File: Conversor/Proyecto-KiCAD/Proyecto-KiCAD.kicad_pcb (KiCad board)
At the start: 2 copper layers, 6 parts, among them Q1 IRFP150, Q2 IRFP150, Q3 IRFP150, Q4 IRFP150, U1 UCC21540, U2 UCC21540

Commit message: Comenzar el layout de componentes de la PCB
- Todos los componentes con footprints asignados (preliminar)
- Organizados los componentes de la placa adaptadora en el esquema del
PCB (usando como guia aproximada la placa adaptadora)
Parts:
- added C1: Csnub1, Capacitor_SMD:C_1206_3216Metric_Pad1.33x1.80mm_HandSolder, F.Cu at (42.6, 256.0)
- added C10: C, Capacitor_SMD:C_1206_3216Metric_Pad1.33x1.80mm_HandSolder, F.Cu at (154.0, 242.6)
- added C11: CDT, Capacitor_SMD:C_1206_3216Metric_Pad1.33x1.80mm_HandSolder, F.Cu at (160.2, 237.2)
- added C12: CDT, Capacitor_SMD:C_1206_3216Metric_Pad1.33x1.80mm_HandSolder, F.Cu at (168.7, 231.0)
- added C13: CVCC, Capacitor_SMD:C_1206_3216Metric_Pad1.33x1.80mm_HandSolder, F.Cu at (148.0, 239.3)
- added C14: CVCC, Capacitor_SMD:C_1206_3216Metric_Pad1.33x1.80mm_HandSolder, F.Cu at (154.0, 239.3)
- added C15: Cboot, Capacitor_SMD:C_1206_3216Metric_Pad1.33x1.80mm_HandSolder, F.Cu at (148.0, 242.6)
- added C16: Cboot, Capacitor_SMD:C_1206_3216Metric_Pad1.33x1.80mm_HandSolder, F.Cu at (180.9, 220.8)
- added C17: CS, Capacitor_SMD:C_1206_3216Metric_Pad1.33x1.80mm_HandSolder, F.Cu at (36.6, 256.0)
- added C18: Cvdd, Capacitor_SMD:C_1206_3216Metric_Pad1.33x1.80mm_HandSolder, F.Cu at (122.1, 261.4)
- added C19: Cvref, Capacitor_SMD:C_1206_3216Metric_Pad1.33x1.80mm_HandSolder, F.Cu at (105.9, 274.8)
- added C2: Csnub2, Capacitor_SMD:C_1206_3216Metric_Pad1.33x1.80mm_HandSolder, F.Cu at (48.6, 256.0)
- added C20: C, Capacitor_SMD:C_1206_3216Metric_Pad1.33x1.80mm_HandSolder, F.Cu at (105.9, 271.4)
- added C21: Cvin, Capacitor_SMD:C_1206_3216Metric_Pad1.33x1.80mm_HandSolder, F.Cu at (110.1, 261.4)
- added C22: C, Capacitor_SMD:C_1206_3216Metric_Pad1.33x1.80mm_HandSolder, F.Cu at (127.0, 254.9)
- added C23: C, Capacitor_SMD:C_1206_3216Metric_Pad1.33x1.80mm_HandSolder, F.Cu at (116.1, 261.4)
- added C24: C4amp, Capacitor_SMD:C_1206_3216Metric_Pad1.33x1.80mm_HandSolder, F.Cu at (111.9, 268.1)
- added C25: C2amp, Capacitor_SMD:C_1206_3216Metric_Pad1.33x1.80mm_HandSolder, F.Cu at (110.1, 264.7)
- added C26: C, Capacitor_SMD:C_1206_3216Metric_Pad1.33x1.80mm_HandSolder, F.Cu at (116.1, 264.7)
- added C27: C, Capacitor_SMD:C_1206_3216Metric_Pad1.33x1.80mm_HandSolder, F.Cu at (105.9, 268.1)
- added C28: CREGIN, Capacitor_SMD:C_1206_3216Metric_Pad1.33x1.80mm_HandSolder, F.Cu at (151.8, 212.6)
- added C29: CREG_IN, Capacitor_SMD:C_1206_3216Metric_Pad1.33x1.80mm_HandSolder, F.Cu at (164.2, 207.0)
- added C3: Csnub3, Capacitor_SMD:C_1206_3216Metric_Pad1.33x1.80mm_HandSolder, F.Cu at (65.4, 245.5)
- added C30: CREG_OUT, Capacitor_SMD:C_1206_3216Metric_Pad1.33x1.80mm_HandSolder, F.Cu at (173.5, 198.3)
- added C31: CFIN, Capacitor_SMD:C_1206_3216Metric_Pad1.33x1.80mm_HandSolder, F.Cu at (181.2, 188.6)
- added C32: CBYPASS, Capacitor_SMD:C_1206_3216Metric_Pad1.33x1.80mm_HandSolder, F.Cu at (145.8, 212.6)
- added C33: CREGOUT, Capacitor_SMD:C_1206_3216Metric_Pad1.33x1.80mm_HandSolder, F.Cu at (157.9, 212.6)
- added C34: 0.1uF, Capacitor_SMD:C_1206_3216Metric_Pad1.33x1.80mm_HandSolder, F.Cu at (368.6, 181.6)
- added C35: 0.1uF, Capacitor_SMD:C_1206_3216Metric_Pad1.33x1.80mm_HandSolder, F.Cu at (373.7, 175.3)
- added C36: 0.1uF, Capacitor_SMD:C_1206_3216Metric_Pad1.33x1.80mm_HandSolder, F.Cu at (358.1, 153.7)
- added C37: 27pF, Capacitor_SMD:C_1206_3216Metric_Pad1.33x1.80mm_HandSolder, F.Cu at (378.5, 167.6)
- added C38: 27pF, Capacitor_SMD:C_1206_3216Metric_Pad1.33x1.80mm_HandSolder, F.Cu at (378.5, 162.6)
- added C39: 1uF, Capacitor_SMD:C_1206_3216Metric_Pad1.33x1.80mm_HandSolder, F.Cu at (337.8, 160.0)
- added C4: Csnub4, Capacitor_SMD:C_1206_3216Metric_Pad1.33x1.80mm_HandSolder, F.Cu at (71.3, 236.1)
- added C40: 10nF, Capacitor_SMD:C_1206_3216Metric_Pad1.33x1.80mm_HandSolder, F.Cu at (364.5, 186.7)
- added C41: 0.1uF, Capacitor_SMD:C_1206_3216Metric_Pad1.33x1.80mm_HandSolder, F.Cu at (342.9, 152.4)
- added C42: 0.1uF, Capacitor_SMD:C_1206_3216Metric_Pad1.33x1.80mm_HandSolder, F.Cu at (339.1, 152.4)
- added C43: 10uF, Capacitor_THT:CP_Radial_D6.3mm_P2.50mm, F.Cu at (331.5, 153.7)
- added C44: 10nF, Capacitor_SMD:C_1206_3216Metric_Pad1.33x1.80mm_HandSolder, F.Cu at (330.2, 163.8)
- added C45: 0.1uF, Capacitor_SMD:C_1206_3216Metric_Pad1.33x1.80mm_HandSolder, F.Cu at (365.8, 161.3)
- added C46: 2.2uF, Capacitor_THT:CP_Radial_D6.3mm_P2.50mm, F.Cu at (341.6, 165.1)
- added C47: 33nF, Capacitor_SMD:C_1206_3216Metric_Pad1.33x1.80mm_HandSolder, F.Cu at (349.2, 162.6)
- added C5: Cin, Capacitor_THT:CP_Radial_D6.3mm_P2.50mm, F.Cu at (83.0, 223.1)
- added C6: Cf, Capacitor_THT:CP_Radial_D18.0mm_P7.50mm, F.Cu at (28.4, 228.9)
- added C7: C, Capacitor_SMD:C_1206_3216Metric_Pad1.33x1.80mm_HandSolder, F.Cu at (160.0, 240.5)
- added C8: C, Capacitor_SMD:C_1206_3216Metric_Pad1.33x1.80mm_HandSolder, F.Cu at (166.2, 237.2)
- added C9: C, Capacitor_SMD:C_1206_3216Metric_Pad1.33x1.80mm_HandSolder, F.Cu at (174.7, 231.0)
- added D1: MUR860, Package_TO_SOT_THT:TO-220F-2_Vertical, F.Cu at (45.3, 229.6)
- added D2: MUR860, Package_TO_SOT_THT:TO-220F-2_Vertical, F.Cu at (45.3, 235.8)
- added D3: MUR860, Package_TO_SOT_THT:TO-220F-2_Vertical, F.Cu at (25.2, 255.7)
- added D4: MUR860, Package_TO_SOT_THT:TO-220F-2_Vertical, F.Cu at (62.7, 223.0)
- added D5: MBR0520, Diode_SMD:D_SOD-123, F.Cu at (123.8, 268.1)
- added J1: ConnPila, TerminalBlock:TerminalBlock_bornier-2_P5.08mm, F.Cu at (42.5, 249.8)
- added J2: ConnTrafoP, TerminalBlock:TerminalBlock_bornier-2_P5.08mm, F.Cu at (68.5, 229.9)
- added J3: ConnTrafoS, TerminalBlock:TerminalBlock_bornier-2_P5.08mm, F.Cu at (54.0, 249.8)
- added J4: ConnLf, TerminalBlock:TerminalBlock_bornier-2_P5.08mm, F.Cu at (60.0, 239.3)
- added J5: ConnCarga, TerminalBlock:TerminalBlock_bornier-2_P5.08mm, F.Cu at (57.0, 230.3)
- added J6: Barrel_Jack_Switch, Connector_BarrelJack:BarrelJack_GCT_DCJ200-10-A_Horizontal, F.Cu at (297.8, 39.3)
- added J7: DIMM100, 5390213-1:TE_5390213-1, F.Cu at (320.0, 119.4)
- added LED1: Led smd, Diode_SMD:D_1206_3216Metric_Pad1.42x1.75mm_HandSolder, F.Cu at (307.3, 106.7)
- added LED2: Led smd, Diode_SMD:D_1206_3216Metric_Pad1.42x1.75mm_HandSolder, F.Cu at (307.3, 111.8)
- added LED3: Led smd, Diode_SMD:D_1206_3216Metric_Pad1.42x1.75mm_HandSolder, F.Cu at (307.3, 116.8)
- added LED4: Led smd, Diode_SMD:D_1206_3216Metric_Pad1.42x1.75mm_HandSolder, F.Cu at (307.3, 121.9)
- added LED5: Led smd, Diode_SMD:D_1206_3216Metric_Pad1.42x1.75mm_HandSolder, F.Cu at (344.2, 179.1)
- added LED6: Led smd, Diode_SMD:D_1206_3216Metric_Pad1.42x1.75mm_HandSolder, F.Cu at (344.2, 175.3)
- added P1: SW_SPDT, Connector_PinHeader_2.54mm:PinHeader_1x03_P2.54mm_Vertical, F.Cu at (175.9, 189.2)
- added P10: Header GPIO, Connector_PinHeader_2.54mm:PinHeader_1x08_P2.54mm_Vertical, F.Cu at (348.6, 106.7)
- added P11: Header SD, Connector_PinSocket_2.54mm:PinSocket_1x06_P2.54mm_Horizontal, F.Cu at (356.9, 121.9)
- added P12: USB-B, Connector_USB:USB_B_Lumberg_2411_02_Horizontal, F.Cu at (359.4, 190.1)
- added P2: 5V Header, Connector_PinHeader_2.54mm:PinHeader_1x02_P2.54mm_Vertical, F.Cu at (188.1, 181.2)
- added P3: 5V Header, Connector_PinHeader_2.54mm:PinHeader_1x02_P2.54mm_Vertical, F.Cu at (168.2, 197.9)
- added P4: Jumper 2, Connector_PinHeader_2.54mm:PinHeader_1x03_P2.54mm_Vertical, F.Cu at (163.6, 197.9)
- added P5: Header 7X2, Connector_PinSocket_2.54mm:PinSocket_2x07_P2.54mm_Vertical, F.Cu at (287.0, 101.6)
- added P6: Header UART, Connector_PinHeader_2.54mm:PinHeader_1x04_P2.54mm_Vertical, F.Cu at (348.0, 133.4)
- added P7: Header I2C, Connector_PinHeader_2.54mm:PinHeader_1x04_P2.54mm_Vertical, F.Cu at (363.2, 133.4)
- added P8: Header PWM, Connector_PinHeader_2.54mm:PinHeader_1x08_P2.54mm_Vertical, F.Cu at (363.2, 78.8)
- added P9: Header ADC, Connector_PinHeader_2.54mm:PinHeader_1x05_P2.54mm_Vertical, F.Cu at (348.0, 82.5)
- added Q5: IRF7425, Package_SO:SOIC-8_3.9x4.9mm_P1.27mm, F.Cu at (364.8, 175.3)
- added R1: RonH, Resistor_SMD:R_1206_3216Metric_Pad1.30x1.75mm_HandSolder, F.Cu at (166.0, 240.5)
- added R10: 0, Resistor_SMD:R_1206_3216Metric_Pad1.30x1.75mm_HandSolder, F.Cu at (164.2, 210.3)
- added R11: Rpu, Resistor_SMD:R_1206_3216Metric_Pad1.30x1.75mm_HandSolder, F.Cu at (117.8, 274.6)
- added R12: R1amp, Resistor_SMD:R_1206_3216Metric_Pad1.30x1.75mm_HandSolder, F.Cu at (117.9, 268.1)
- added R13: R3amp, Resistor_SMD:R_1206_3216Metric_Pad1.30x1.75mm_HandSolder, F.Cu at (128.0, 264.8)
- added R14: R4amp, Resistor_SMD:R_1206_3216Metric_Pad1.30x1.75mm_HandSolder, F.Cu at (117.9, 271.3)
- added R15: 0, Resistor_SMD:R_1206_3216Metric_Pad1.30x1.75mm_HandSolder, F.Cu at (188.7, 187.7)
- added R16: R2amp, Resistor_SMD:R_1206_3216Metric_Pad1.30x1.75mm_HandSolder, F.Cu at (132.9, 254.9)
- added R17: 0, Resistor_SMD:R_1206_3216Metric_Pad1.30x1.75mm_HandSolder, F.Cu at (193.4, 180.5)
- added R18: Rpu, Resistor_SMD:R_1206_3216Metric_Pad1.30x1.75mm_HandSolder, F.Cu at (128.1, 261.5)
- added R19: Rpu, Resistor_SMD:R_1206_3216Metric_Pad1.30x1.75mm_HandSolder, F.Cu at (122.1, 264.7)
- added R2: RonL, Resistor_SMD:R_1206_3216Metric_Pad1.30x1.75mm_HandSolder, F.Cu at (180.9, 224.2)
- added R20: R, Resistor_SMD:R_1206_3216Metric_Pad1.30x1.75mm_HandSolder, F.Cu at (128.1, 258.2)
- added R21: 220, Resistor_SMD:R_1206_3216Metric_Pad1.30x1.75mm_HandSolder, F.Cu at (301.2, 106.7)
- added R22: 1k, Resistor_SMD:R_1206_3216Metric_Pad1.30x1.75mm_HandSolder, F.Cu at (281.8, 129.8)
- added R23: 220, Resistor_SMD:R_1206_3216Metric_Pad1.30x1.75mm_HandSolder, F.Cu at (301.2, 111.8)
- added R24: 1k, Resistor_SMD:R_1206_3216Metric_Pad1.30x1.75mm_HandSolder, F.Cu at (281.8, 140.2)
- added R25: 220, Resistor_SMD:R_1206_3216Metric_Pad1.30x1.75mm_HandSolder, F.Cu at (301.2, 116.8)
- added R26: 1k, Resistor_SMD:R_1206_3216Metric_Pad1.30x1.75mm_HandSolder, F.Cu at (281.8, 150.4)
- added R27: 220, Resistor_SMD:R_1206_3216Metric_Pad1.30x1.75mm_HandSolder, F.Cu at (301.2, 121.9)
- added R28: 1k, Resistor_SMD:R_1206_3216Metric_Pad1.30x1.75mm_HandSolder, F.Cu at (281.8, 160.6)
- added R29: 1k, Resistor_SMD:R_1206_3216Metric_Pad1.30x1.75mm_HandSolder, F.Cu at (362.2, 181.6)
- added R3: RonH, Resistor_SMD:R_1206_3216Metric_Pad1.30x1.75mm_HandSolder, F.Cu at (180.9, 227.4)
- added R30: 470, Resistor_SMD:R_1206_3216Metric_Pad1.30x1.75mm_HandSolder, F.Cu at (132.6, 241.8)
- added R31: 1k, Resistor_SMD:R_1206_3216Metric_Pad1.30x1.75mm_HandSolder, F.Cu at (349.2, 156.2)
- added R32: 27, Resistor_SMD:R_1206_3216Metric_Pad1.30x1.75mm_HandSolder, F.Cu at (356.2, 184.4)
- added R33: 27, Resistor_SMD:R_1206_3216Metric_Pad1.30x1.75mm_HandSolder, F.Cu at (353.1, 184.4)
- added R34: 1k5, Resistor_SMD:R_1206_3216Metric_Pad1.30x1.75mm_HandSolder, F.Cu at (351.5, 179.5)
- added R35: 220, Resistor_SMD:R_1206_3216Metric_Pad1.30x1.75mm_HandSolder, F.Cu at (337.8, 179.1)
- added R36: 220, Resistor_SMD:R_1206_3216Metric_Pad1.30x1.75mm_HandSolder, F.Cu at (337.8, 175.3)
- added R37: Rfix, Resistor_SMD:R_1206_3216Metric_Pad1.30x1.75mm_HandSolder, F.Cu at (181.2, 191.9)
- added R38: Rfix, Resistor_SMD:R_1206_3216Metric_Pad1.30x1.75mm_HandSolder, F.Cu at (111.9, 271.4)
- added R4: RonL, Resistor_SMD:R_1206_3216Metric_Pad1.30x1.75mm_HandSolder, F.Cu at (180.7, 231.0)
- added R5: RS, Resistor_SMD:R_1206_3216Metric_Pad1.30x1.75mm_HandSolder, F.Cu at (172.2, 234.4)
- added R6: RS, Resistor_SMD:R_1206_3216Metric_Pad1.30x1.75mm_HandSolder, F.Cu at (186.9, 220.8)
- added R7: RS, Resistor_SMD:R_2512_6332Metric_Pad1.40x3.35mm_HandSolder, F.Cu at (75.7, 221.6)
- added R8: Rpu, Resistor_SMD:R_1206_3216Metric_Pad1.30x1.75mm_HandSolder, F.Cu at (111.9, 274.7)
- added R9: Rpu, Resistor_SMD:R_1206_3216Metric_Pad1.30x1.75mm_HandSolder, F.Cu at (134.0, 258.2)
- added SW1: Switch, Button_Switch_THT:SW_PUSH_6mm, F.Cu at (294.6, 134.3)
- added SW2: Switch, Button_Switch_THT:SW_PUSH_6mm, F.Cu at (294.6, 144.8)
- added SW3: Switch, Button_Switch_THT:SW_PUSH_6mm, F.Cu at (294.6, 154.9)
- added SW4: Switch, Button_Switch_THT:SW_PUSH_6mm, F.Cu at (294.6, 165.1)
- added SW5: Switch, Button_Switch_THT:SW_PUSH_6mm, F.Cu at (362.5, 151.4)
- added U10: OPA365xxD, Package_SO:SOIC-8_3.9x4.9mm_P1.27mm, F.Cu at (111.3, 256.5)
- added U11: LM7805_TO252, Package_TO_SOT_SMD:TO-252-2, F.Cu at (179.7, 182.9)
- added U12: ACPL-P480, Package_SO:SSO-6_6.8x4.6mm_P1.27mm_Clearance7mm, F.Cu at (163.3, 222.2)
- added U13: THB3-1211, Package_DIP:DIP-24_W15.24mm, F.Cu at (289.6, 49.5)
- added U14: FT232BL, Package_QFP:LQFP-48_7x7mm_P0.5mm, F.Cu at (358.1, 165.1)
- added U15: LP2985-3.3, Package_TO_SOT_SMD:SOT-23-5, F.Cu at (335.4, 164.5)
- added U3: ACPL-P480, Package_SO:SSO-6_6.8x4.6mm_P1.27mm_Clearance7mm, F.Cu at (151.1, 234.5)
- added U4: ACPL-P480, Package_SO:SSO-6_6.8x4.6mm_P1.27mm_Clearance7mm, F.Cu at (151.1, 222.2)
- added U5: 2ED21834-S06J, Package_SO:SO-14_3.9x8.65mm_P1.27mm, F.Cu at (161.4, 230.4)
- added U6: 2ED21834-S06J, Package_SO:SO-14_3.9x8.65mm_P1.27mm, F.Cu at (173.7, 224.3)
- added U7: TMCS1100A4, Package_SO:SOIC-8_3.9x4.9mm_P1.27mm, F.Cu at (119.7, 256.5)
- added U8: LM5056APMH/NOPB, Package_SO:HTSSOP-28-1EP_4.4x9.7mm_P0.65mm_EP2.85x5.4mm, F.Cu at (98.5, 270.7)
- added U9: ISO7242C, Package_SO:SOIC-16W_7.5x10.3mm_P1.27mm, F.Cu at (100.6, 259.2)
- added Y1: 6 MHz, Crystal:Crystal_HC18-U_Vertical, F.Cu at (370.8, 167.6)
- Q1, Q2, Q3, Q4: footprint Package_TO_SOT_THT:TO-247-3_Horizontal_TabDown -> Package_TO_SOT_THT:TO-247-3_Vertical
- U1: value UCC21540 -> LP2985-3.3; footprint Package_SO:SOIC-16W_7.5x10.3mm_P1.27mm -> Package_TO_SOT_SMD:SOT-23-5
- U2: value UCC21540 -> ACPL-P480; footprint Package_SO:SOIC-16W_7.5x10.3mm_P1.27mm -> Package_SO:SSO-6_6.8x4.6mm_P1.27mm_Clearance7mm
- moved Q1 180.8 mm to (25.1, 241.8)
- moved Q4 180.8 mm to (42.5, 241.8)
- moved Q2 164.7 mm to (25.1, 248.4)
- moved Q3 141.7 mm to (45.2, 222.3)
- moved U2 112.4 mm to (151.1, 228.4)
- moved U1 101.0 mm to (180.8, 195.8)
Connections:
- Q1 pad 1: Net-(Q1-Pad1) -> Net-(C1-Pad1)
- Q1 pad 2: Net-(Q1-Pad2) -> /Conversor/GATE1
- Q1 pad 3: Net-(Q1-Pad3) -> /Conversor/S1D3
- Q2 pad 1: Net-(Q1-Pad3) -> Net-(C1-Pad1)
- Q2 pad 2: Net-(Q2-Pad2) -> /Conversor/GATE2
- Q2 pad 3: Net-(Q2-Pad3) -> /Conversor/S2D4
- Q3 pad 1: Net-(Q1-Pad1) -> /Conversor/S1D3
- Q3 pad 2: Net-(Q3-Pad2) -> /Conversor/GATE3
- Q3 pad 3: Net-(Q3-Pad3) -> GND1
- Q4 pad 1: Net-(Q3-Pad3) -> /Conversor/S2D4
- Q4 pad 2: Net-(Q4-Pad2) -> /Conversor/GATE4
- Q4 pad 3: Net-(Q2-Pad3) -> GND1
- U1 pad 1: unconnected-(U1-Pad1) -> +5VD
- U1 pad 2: unconnected-(U1-Pad2) -> GNDD
- U1 pad 3: unconnected-(U1-Pad3) -> +5VD
- U1 pad 4: unconnected-(U1-Pad4) -> Net-(C32-Pad1)
- U1 pad 5: unconnected-(U1-Pad5) -> +3.3V
- U2 pad 1: unconnected-(U2-Pad1) -> /Drivers y Optos/PWM1
- U2 pad 3: unconnected-(U2-Pad3) -> GNDD
- U2 pad 4: unconnected-(U2-Pad4) -> GND1
- U2 pad 5: unconnected-(U2-Pad5) -> (no net)
- U2 pad 6: unconnected-(U2-Pad6) -> +5VP

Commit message: Reempezar el ordenado de componentes del PCB
- Intentar copiar mas a la placa adaptadora en la parte del DSP (digital)
  - Algunas cosas (como los headers y la parte de USB) se movieron para hacer entrar mejor las cosas
- Layout bastante completo
- Agregados algunos modelos 3D faltantes
Por hacer:
  - Mover y reorganizar la parte del LM5056, porque tiene una pata que va al secundario, y ahora esta muy lejos del area de GND2
  - Ver como reorganizar un poco para que no queden esquinas vacias
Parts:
- added R39: Rfix, Resistor_SMD:R_1206_3216Metric_Pad1.30x1.75mm_HandSolder, F.Cu at (104.1, 216.5)
- added R7: RS, Resistor_SMD:R_2512_6332Metric_Pad1.40x3.35mm_HandSolder, F.Cu at (67.9, 203.2)
- C10, C17, C18, C19, C34, C36, C37, C38, C40, C45, C47, C7, C8, C9, R1, R10, R15, R17, R19, R2, R29, R3, R31, R4, R9: moved to B.Cu
- C43: footprint Capacitor_THT:CP_Radial_D6.3mm_P2.50mm -> Capacitor_THT:CP_Radial_D4.0mm_P1.50mm
- C46: footprint Capacitor_THT:CP_Radial_D6.3mm_P2.50mm -> Capacitor_THT:CP_Radial_D4.0mm_P2.00mm
- U14: footprint Package_QFP:LQFP-48_7x7mm_P0.5mm -> Package_DFN_QFN:QFN-32-1EP_7x7mm_P0.65mm_EP5.4x5.4mm
- moved C38 262.0 mm to (116.8, 176.5), turned to 90 degrees
- moved C37 256.7 mm to (121.9, 176.5), turned to 90 degrees
- moved Y1 251.9 mm to (119.4, 183.0), turned to -90 degrees
- moved C45 238.5 mm to (129.0, 190.0), turned to 180 degrees
- moved SW5 235.9 mm to (127.6, 173.0)
- moved D3 231.6 mm to (150.6, 61.0), turned to 90 degrees
- moved P8 231.4 mm to (140.3, 141.0)
- moved C40 230.5 mm to (134.6, 203.2)
- moved LED6 227.3 mm to (118.1, 198.8), turned to -90 degrees
- moved U14 226.7 mm to (132.7, 188.5), turned to 90 degrees
- moved P12 226.7 mm to (133.3, 206.6)
- moved LED5 224.4 mm to (120.7, 198.8), turned to -90 degrees
- moved R36 221.7 mm to (118.1, 205.1), turned to 90 degrees
- moved R34 221.4 mm to (130.8, 196.8), turned to 90 degrees
- moved J3 221.0 mm to (160.0, 55.9)
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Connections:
- C1 pad 1: Net-(C1-Pad1) -> /Conversor/IFC-
- C17 pad 1: /Conversor/IFC+ -> /Conversor/VFC
- C2 pad 1: Net-(C1-Pad1) -> /Conversor/IFC-
- C33 pad 1: +3.3V -> +3V3
- C5 pad 1: Net-(C1-Pad1) -> /Conversor/IFC-
- D1 pad 1: (no net) -> Net-(D1-Pad1)
- D1 pad 2: (no net) -> Net-(D1-Pad2)
- D2 pad 1: (no net) -> Net-(D2-Pad1)
- D2 pad 2: (no net) -> Net-(D1-Pad2)
- D3 pad 1: (no net) -> GND2
- D3 pad 2: (no net) -> Net-(D1-Pad1)
- D4 pad 1: (no net) -> GND2
- D4 pad 2: (no net) -> Net-(D2-Pad1)
- J3 pad 1: Net-(D1-Pad3) -> Net-(D1-Pad1)
- J3 pad 2: Net-(D2-Pad3) -> Net-(D2-Pad1)
- J4 pad 1: Net-(D1-Pad4) -> Net-(D1-Pad2)
- Q1 pad 1: Net-(C1-Pad1) -> /Conversor/IFC-
- Q2 pad 1: Net-(C1-Pad1) -> /Conversor/IFC-
- U1 pad 5: +3.3V -> +3V3
- U12 pad 5: (no net) -> Net-(U12-Pad5)
- U2 pad 5: (no net) -> Net-(U2-Pad5)
- U3 pad 5: (no net) -> Net-(U3-Pad5)
- U4 pad 5: (no net) -> Net-(U4-Pad5)
- U5 pad 1: Net-(U2-Pad4) -> Net-(U2-Pad5)
- U5 pad 2: Net-(U3-Pad4) -> Net-(U3-Pad5)
- U6 pad 1: Net-(U4-Pad4) -> Net-(U4-Pad5)
- U6 pad 2: Net-(U12-Pad4) -> Net-(U12-Pad5)
- U8 pad 16: (no net) -> Net-(R38-Pad1)
- U8 pad 22: (no net) -> Net-(U8-Pad22)
- U8 pad 4: /Conversor/IFC+ -> /Conversor/VFC

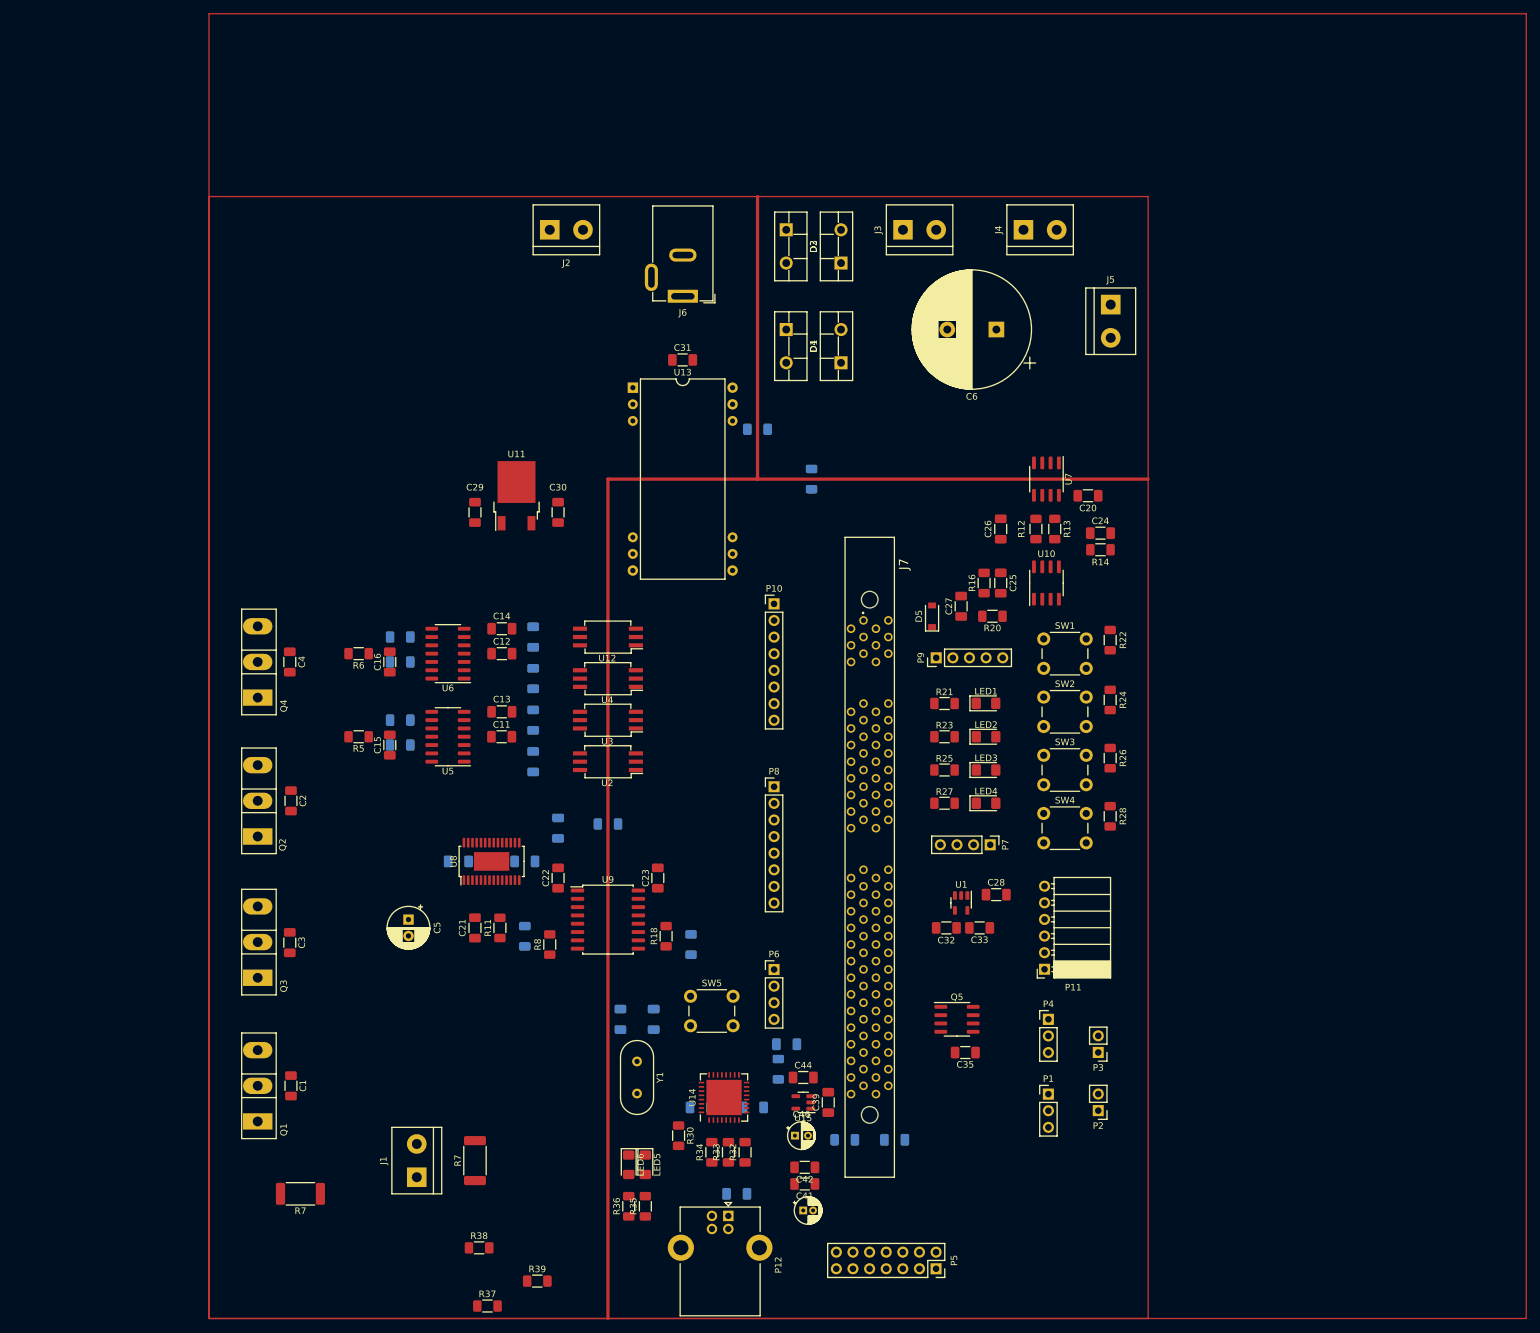
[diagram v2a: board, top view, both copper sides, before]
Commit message: Terminar la parte digital de la PCB (incluidas las pistas)
- Hay que ver si la clearance de 0.254mm para el plano de GNDD esta bien
- Cambiar la footprint del FTDI por la version correcta
- Borrar R37, R38 y R39 (usadas para corregir errores del ERC)
Por hacer:
  - Terminar las otras dos partes de la placa
  - Consultar si esta bien lo que hice hasta ahora
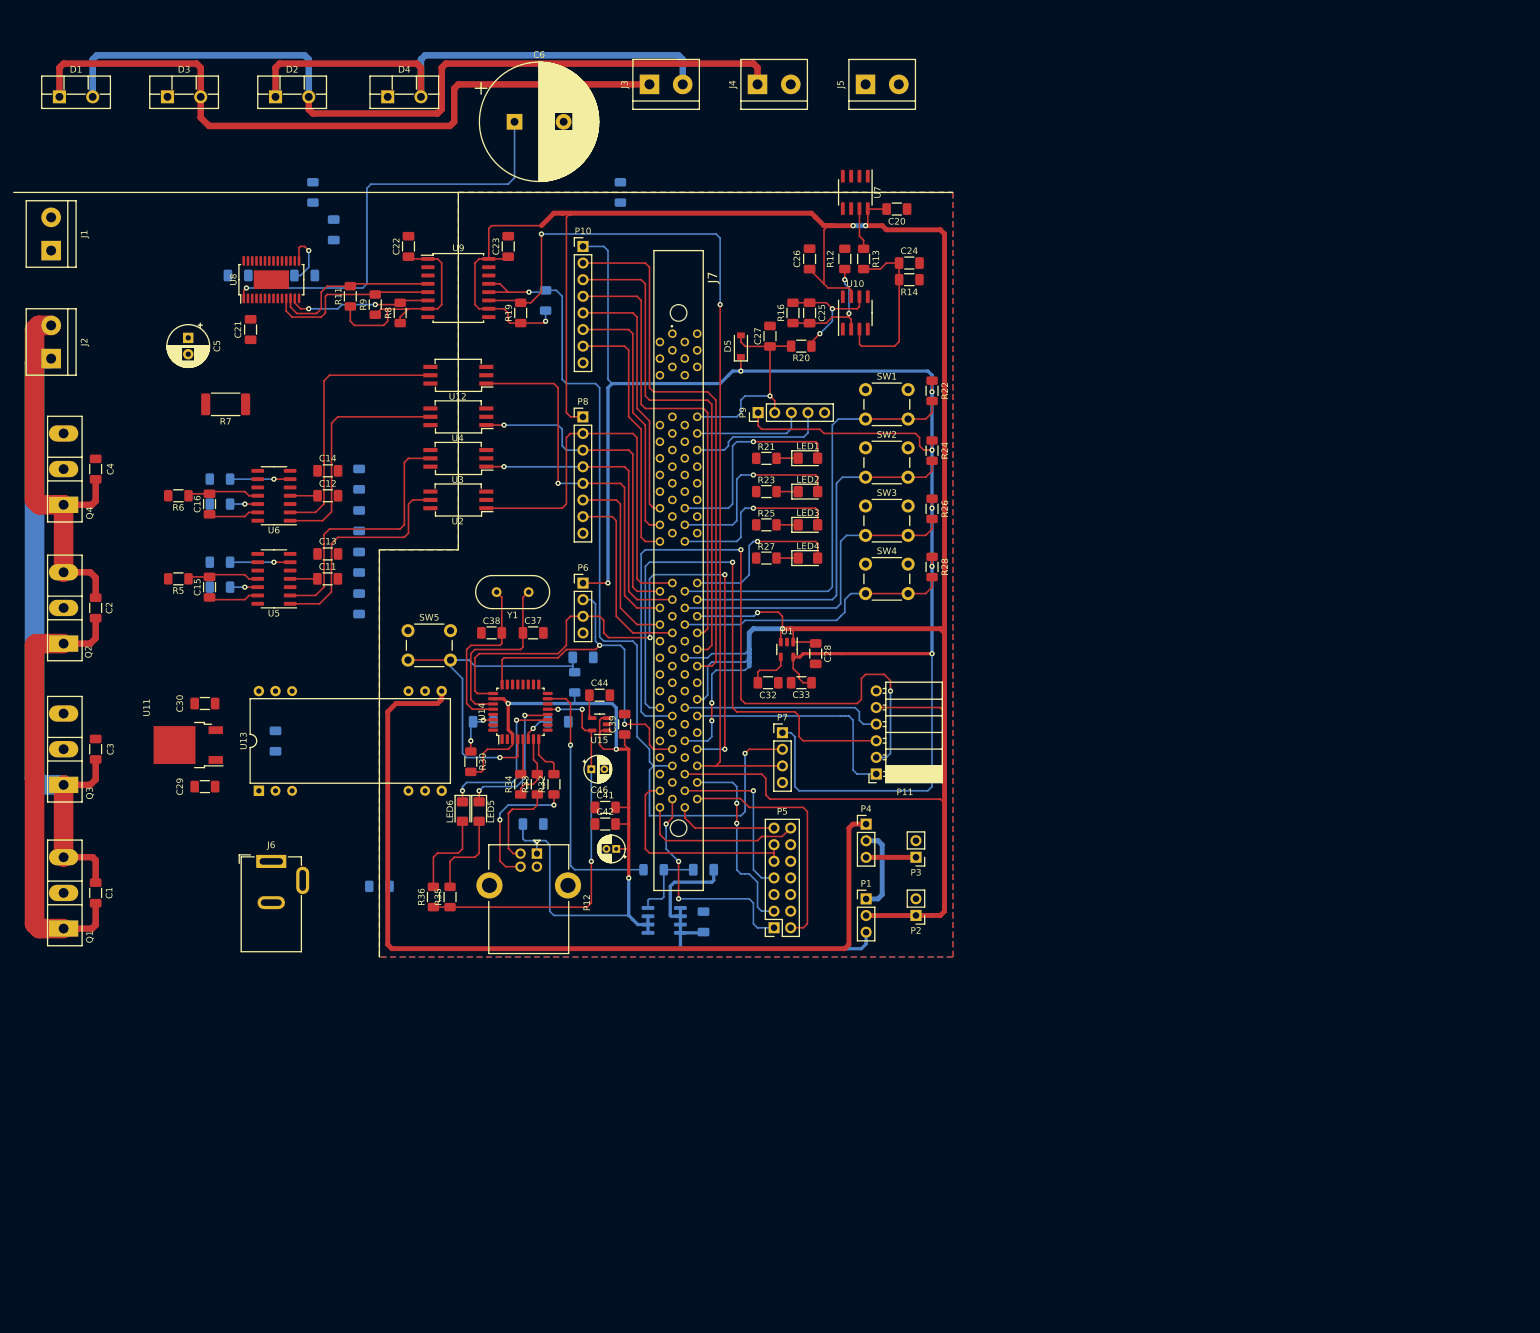
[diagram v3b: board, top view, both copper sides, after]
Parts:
- removed R37, R38, R39: Rfix, Resistor_SMD:R_1206_3216Metric_Pad1.30x1.75mm_HandSolder
- removed the R7 at (94.6, 198.1)
- C31, C35, Q5, R18: moved to B.Cu
- C37, C38, R19, R9: moved to F.Cu
- U14: footprint Package_DFN_QFN:QFN-32-1EP_7x7mm_P0.65mm_EP5.4x5.4mm -> Package_QFP:LQFP-32_7x7mm_P0.8mm
- moved J1 152.2 mm to (29.8, 59.1)
- moved D1 126.2 mm to (31.1, 35.6), turned to 0 degrees
- moved R7 121.2 mm to (56.5, 82.5)
- moved J6 106.8 mm to (63.5, 152.4), turned to 0 degrees
- moved D3 106.0 mm to (47.6, 35.6), turned to 0 degrees
- moved R19 100.0 mm to (101.6, 68.6)
- moved R9 99.2 mm to (79.4, 67.3)
- moved C22 99.2 mm to (84.5, 58.4)
- moved C23 99.2 mm to (99.7, 58.4)
- moved R11 99.2 mm to (75.6, 66.0)
- moved R8 99.2 mm to (83.2, 68.6)
- moved U9 99.2 mm to (92.1, 64.8)
- moved R18 98.9 mm to (105.4, 66.7)
- moved C18 97.7 mm to (73.0, 55.9)
- moved C21 97.7 mm to (60.3, 71.1)
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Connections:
- C17 pad 1: /Conversor/VFC -> /Conversor/IFC+
- C21 pad 1: /Conversor/VFC -> /Conversor/IFC+
- J1 pad 1: /Conversor/VFC -> /Conversor/IFC+
- J7 pad 81: unconnected-(J7-Pad81) -> /Placa DSP/Socket Interfaces/GPIO-85
- P10 pad 2: /Placa DSP/Socket Interfaces/GPIO-11 -> /Placa DSP/Socket Interfaces/GPIO-13
- P10 pad 3: /Placa DSP/Socket Interfaces/GPIO-13 -> /Placa DSP/Socket Interfaces/GPIO-85
- P10 pad 4: /Placa DSP/Socket Interfaces/GPIO-49 -> /Placa DSP/Socket Interfaces/GPIO-11
- R7 pad 1: /Conversor/VFC -> /Conversor/IFC+
- U13 pad 12: Net-(R37-Pad1) -> GNDD
- U8 pad 16: Net-(R38-Pad1) -> GND1
- U8 pad 22: Net-(U8-Pad22) -> GND1
- U8 pad 4: /Conversor/VFC -> /Conversor/IFC+
- U8 pad 5: /Conversor/VFC -> /Conversor/IFC+
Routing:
- net +5VD: track 0.00 -> 432.5 mm, vias 0 -> 7
- net +3V3: track 0.00 -> 269.7 mm, vias 0 -> 7
- net /Conversor/S2D4: track 0.00 -> 159.7 mm
- net /Placa DSP/Socket Interfaces/I2CSCL: track 0.00 -> 139.9 mm, vias 0 -> 2
- net /Placa DSP/Socket Interfaces/I2CSDA: track 0.00 -> 138.4 mm, vias 0 -> 2
- net /Fuentes/+5VD ISO: track 0.00 -> 137.5 mm
- net /Placa DSP/USB-UART/U5V: track 0.00 -> 126.0 mm, vias 0 -> 3
- net Net-(D1-Pad2): track 0.00 -> 125.4 mm
- net Net-(D1-Pad1): track 0.00 -> 108.9 mm
- net /Placa DSP/Socket Interfaces/SPI-CLK: track 0.00 -> 108.3 mm, vias 0 -> 2
- net /Placa DSP/Socket Interfaces/SCI-TX: track 0.00 -> 93.8 mm, vias 0 -> 3
- net /Placa DSP/Socket Interfaces/SPI-SIMO: track 0.00 -> 85.2 mm, vias 0 -> 1
- net /Placa DSP/Socket Interfaces/GPIO-13: track 0.00 -> 82.9 mm
- net Net-(D2-Pad1): track 0.00 -> 81.7 mm
- net /Placa DSP/Socket Interfaces/GPIO-85: track 0.00 -> 76.9 mm
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- added copper zone on B.Cu, net GNDD
- added copper zone on F.Cu, net GNDD
